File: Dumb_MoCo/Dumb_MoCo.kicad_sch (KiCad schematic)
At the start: 18 parts, among them U1 VNH7070AS

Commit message: Completed layout before review
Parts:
- removed C3: 220uF, symbol Device:C
- removed Conn3: Molex_SL_02, symbol MRDT_Connectors:Molex_SL_02
- removed Conn4: Molex_SL_03, symbol MRDT_Connectors:Molex_SL_03
- added C3: 270uF, Capacitor_THT:CP_Radial_D8.0mm_P3.50mm, symbol Device:C_Polarized
- added C4: 10nF, Capacitor_SMD:C_0603_1608Metric_Pad1.08x0.95mm_HandSolder, symbol Device:C
- added Conn3: Molex_SL_05, MRDT_Connectors:MOLEX_SL_05_Horizontal, symbol MRDT_Connectors:Molex_SL_05
- C1, C2: footprint (none) -> Capacitor_SMD:C_0603_1608Metric_Pad1.08x0.95mm_HandSolder
- Conn1, Conn2: footprint (none) -> MRDT_Connectors:Square_Anderson_2_H_Side_By_Side
- U1: footprint (none) -> Package_SO:SOIC-16_3.9x9.9mm_P1.27mm
- V1, V2, V3, V4: footprint (none) -> MRDT_Drill_Holes:4_40_Hole
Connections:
- net +12V: now also C3.1
- net CS: now also C4.2, Conn3.2
- net GND: now also C3.2, C4.1
- net IN_A: now also Conn3.3
- net IN_B: now also Conn3.4
- net M-: now also Conn1.1 (GND), U1.10 (OUT_B), U1.7 (OUT_B)
- net PWM: now also Conn3.5
- net SEL: now also Conn3.1
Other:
- moved on the sheet: Conn1A, Conn1B, R1, R2, R3, R4, R5, R6, V4

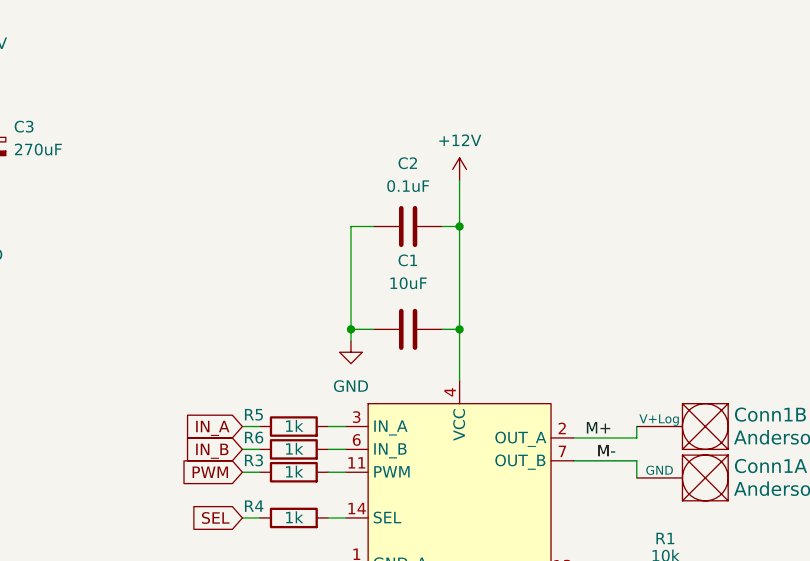
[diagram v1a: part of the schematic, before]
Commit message: Removed C1
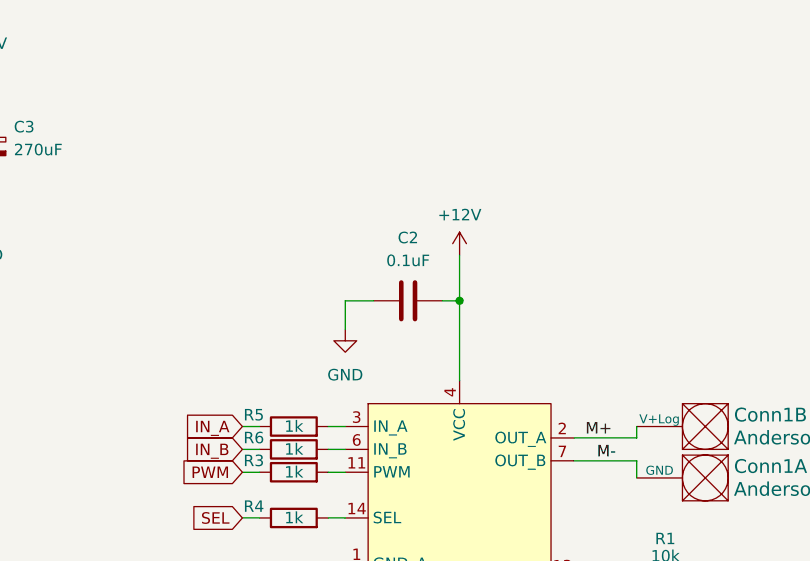
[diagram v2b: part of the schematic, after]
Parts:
- removed C1: 10uF, Capacitor_SMD:C_0603_1608Metric_Pad1.08x0.95mm_HandSolder, symbol Device:C
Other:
- moved on the sheet: C2
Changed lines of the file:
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@@
 	)
 	(junction
-		(at 92.71 46.355)
+		(at 92.71 54.61)
 		(diameter 0)
 		(color 0 0 0 0)
@@
 	)
 	(junction
-		(at 92.71 57.785)
-		(diameter 0)
-		(color 0 0 0 0)
-	)
-	(junction
-		(at 80.645 57.785)
-		(diameter 0)
-		(color 0 0 0 0)
-	)
-	(junction
 		(at 108.585 85.09)
 		(diameter 0)
@@
 	(wire
 		(pts
-			(xy 80.645 46.355) (xy 80.645 57.785)
-		)
-		(stroke
-			(width 0)
-			(type default)
-		)
-	)
-	(wire
-		(pts
 			(xy 78.105 71.12) (xy 80.01 71.12)
 		)
@@
 	(wire
 		(pts
-			(xy 92.71 57.785) (xy 92.71 63.5)
-		)
-		(stroke
-			(width 0)
-			(type default)
-		)
-	)
-	(wire
-		(pts
-			(xy 80.645 57.785) (xy 83.185 57.785)
-		)
-		(stroke
-			(width 0)
-			(type default)
-		)
-	)
-	(wire
-		(pts
 			(xy 74.93 83.82) (xy 74.93 86.36)
 		)
@@
 	(wire
 		(pts
-			(xy 80.645 57.785) (xy 80.645 59.055)
-		)
-		(stroke
-			(width 0)
-			(type default)
-		)
-	)
-	(wire
-		(pts
-			(xy 90.805 57.785) (xy 92.71 57.785)
-		)
-		(stroke
-			(width 0)
-			(type default)
-		)
-	)
-	(wire
-		(pts
-			(xy 92.71 41.275) (xy 92.71 46.355)
+			(xy 80.01 54.61) (xy 80.01 57.785)
+		)
+		(stroke
+			(width 0)
+			(type default)
+		)
+	)
+	(wire
+		(pts
+			(xy 92.71 49.53) (xy 92.71 54.61)
 		)
 		(stroke
@@
 	(wire
 		(pts
-			(xy 90.805 46.355) (xy 92.71 46.355)
+			(xy 90.805 54.61) (xy 92.71 54.61)
 		)
 		(stroke
@@
 	(wire
 		(pts
+			(xy 92.71 54.61) (xy 92.71 63.5)
+		)
+		(stroke
+			(width 0)
+			(type default)
+		)
+	)
+	(wire
+		(pts
 			(xy 105.41 85.09) (xy 108.585 85.09)
 		)
@@
 	(wire
 		(pts
-			(xy 83.185 46.355) (xy 80.645 46.355)
+			(xy 83.185 54.61) (xy 80.01 54.61)
 		)
 		(stroke
@@
 		(pts
 			(xy 78.105 68.58) (xy 80.01 68.58)
-		)
-		(stroke
-			(width 0)
-			(type default)
-		)
-	)
-	(wire
-		(pts
-			(xy 92.71 46.355) (xy 92.71 57.785)
 		)
 		(stroke
@@
 	(symbol
 		(lib_id "Device:C")
-		(at 86.995 57.785 90)
+		(at 86.995 54.61 90)
 		(unit 1)
 		(exclude_from_sim no)
@@
 		(dnp no)
 		(fields_autoplaced yes)
-		(property "Reference" "C1"
+		(property "Reference" "C2"
+			(at 86.995 47.625 90)
+			(effects
+				(font
+					(size 1.27 1.27)
+				)
+			)
+		)
+		(property "Value" "0.1uF"
 			(at 86.995 50.165 90)
 			(effects
@@
 			)
 		)
-		(property "Value" "10uF"
-			(at 86.995 52.705 90)
-			(effects
-				(font
-					(size 1.27 1.27)
-				)
-			)
-		)
 		(property "Footprint" "Capacitor_SMD:C_0603_1608Metric_Pad1.08x0.95mm_HandSolder"
-			(at 90.805 56.8198 0)
+			(at 90.805 53.6448 0)
 			(effects
 				(font
@@
 		)
 		(property "Datasheet" "~"
-			(at 86.995 57.785 0)
+			(at 86.995 54.61 0)
 			(effects
 				(font
@@
 		)
 		(property "Description" ""
-			(at 86.995 57.785 0)
-			(effects
-				(font
-					(size 1.27 1.27)
-				)
-				(hide yes)
-			)
-		)
-		(pin "1"
-		)
-		(pin "2"
-		)
-		(instances
-			(project "Dumb_MoCo"
-				(path "/e8f67502-d0e6-4aae-8b76-a782f13abdd3"
-					(reference "C1")
-					(unit 1)
-				)
-			)
-		)
-	)
-	(symbol
-		(lib_id "Device:C")
-		(at 86.995 46.355 90)
-		(unit 1)
-		(exclude_from_sim no)
-		(in_bom yes)
-		(on_board yes)
-		(dnp no)
-		(fields_autoplaced yes)
-		(property "Reference" "C2"
-			(at 86.995 39.37 90)
-			(effects
-				(font
-					(size 1.27 1.27)
-				)
-			)
-		)
-		(property "Value" "0.1uF"
-			(at 86.995 41.91 90)
-			(effects
-				(font
-					(size 1.27 1.27)
-				)
-			)
-		)
-		(property "Footprint" "Capacitor_SMD:C_0603_1608Metric_Pad1.08x0.95mm_HandSolder"
-			(at 90.805 45.3898 0)
-			(effects
-				(font
-					(size 1.27 1.27)
-				)
-				(hide yes)
-			)
-		)
-		(property "Datasheet" "~"
-			(at 86.995 46.355 0)
-			(effects
-				(font
-					(size 1.27 1.27)
-				)
-				(hide yes)
-			)
-		)
-		(property "Description" ""
-			(at 86.995 46.355 0)
+			(at 86.995 54.61 0)
 			(effects
 				(font
@@
 	(symbol
 		(lib_id "power:+12V")
-		(at 92.71 41.275 0)
+		(at 92.71 49.53 0)
 		(unit 1)
 		(exclude_from_sim no)
@@
 		(fields_autoplaced yes)
 		(property "Reference" "#PWR02"
+			(at 92.71 53.34 0)
+			(effects
+				(font
+					(size 1.27 1.27)
+				)
+				(hide yes)
+			)
+		)
+		(property "Value" "+12V"
 			(at 92.71 45.085 0)
 			(effects
@@
 					(size 1.27 1.27)
 				)
-				(hide yes)
-			)
-		)
-		(property "Value" "+12V"
-			(at 92.71 36.83 0)
-			(effects
-				(font
-					(size 1.27 1.27)
-				)
 			)
 		)
 		(property "Footprint" ""
-			(at 92.71 41.275 0)
+			(at 92.71 49.53 0)
 			(effects
 				(font
@@
 		)
 		(property "Datasheet" ""
-			(at 92.71 41.275 0)
+			(at 92.71 49.53 0)
 			(effects
 				(font
@@
 		)
 		(property "Description" ""
-			(at 92.71 41.275 0)
+			(at 92.71 49.53 0)
 			(effects
 				(font
@@
 	(symbol
 		(lib_id "power:GND")
-		(at 80.645 59.055 0)
+		(at 80.01 57.785 0)
 		(unit 1)
 		(exclude_from_sim no)
@@
 		(dnp no)
 		(property "Reference" "#PWR01"
-			(at 80.645 65.405 0)
+			(at 80.01 64.135 0)
 			(effects
 				(font
@@
 		)
 		(property "Value" "GND"
-			(at 80.645 64.135 0)
+			(at 80.01 62.865 0)
 			(effects
 				(font
@@
 		)
 		(property "Footprint" ""
-			(at 80.645 59.055 0)
+			(at 80.01 57.785 0)
 			(effects
 				(font
@@
 		)
 		(property "Datasheet" ""
-			(at 80.645 59.055 0)
+			(at 80.01 57.785 0)
 			(effects
 				(font
@@
 		)
 		(property "Description" ""
-			(at 80.645 59.055 0)
-			(effects
-				(font
+			(at 80.01 57.785 0)
+			(effects
+				(font

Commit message: Added Chamber Ult Silkscreen
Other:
- moved on the sheet: C2, C4, Conn1A, Conn1B, Conn3, R1, R2, R3, R4, R5, R6, U1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

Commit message: Started on layout
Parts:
- removed V1, V2, V3, V4: Via, MRDT_Drill_Holes:4_40_Hole, symbol MRDT_Drill_Holes:Via

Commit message: Finished layout draft
made anderson and SL vertical
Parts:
- Conn2: footprint MRDT_Connectors:Square_Anderson_2_H_Side_By_Side -> MRDT_Connectors:Square_Anderson_2_V_Side_By_Side
- Conn3: footprint MRDT_Connectors:MOLEX_SL_05_Horizontal -> MRDT_Connectors:MOLEX_SL_05_Vertical
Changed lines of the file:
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@@
 			)
 		)
-		(property "Footprint" "MRDT_Connectors:Square_Anderson_2_H_Side_By_Side"
+		(property "Footprint" "MRDT_Connectors:Square_Anderson_2_V_Side_By_Side"
 			(at 23.495 59.69 0)
 			(effects
@@
 			)
 		)
-		(property "Footprint" "MRDT_Connectors:MOLEX_SL_05_Horizontal"
+		(property "Footprint" "MRDT_Connectors:MOLEX_SL_05_Vertical"
 			(at 38.1 68.58 0)
 			(effects
@@
 			)
 		)
-		(property "Footprint" "MRDT_Connectors:Square_Anderson_2_H_Side_By_Side"
+		(property "Footprint" "MRDT_Connectors:Square_Anderson_2_V_Side_By_Side"
 			(at 23.495 48.26 0)
 			(effects

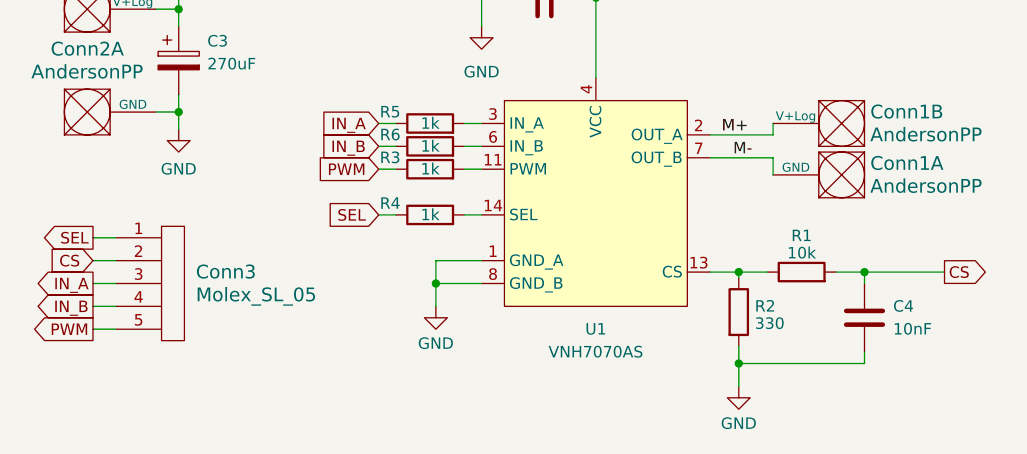
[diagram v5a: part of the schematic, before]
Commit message: Flipped VNH and reordered SL
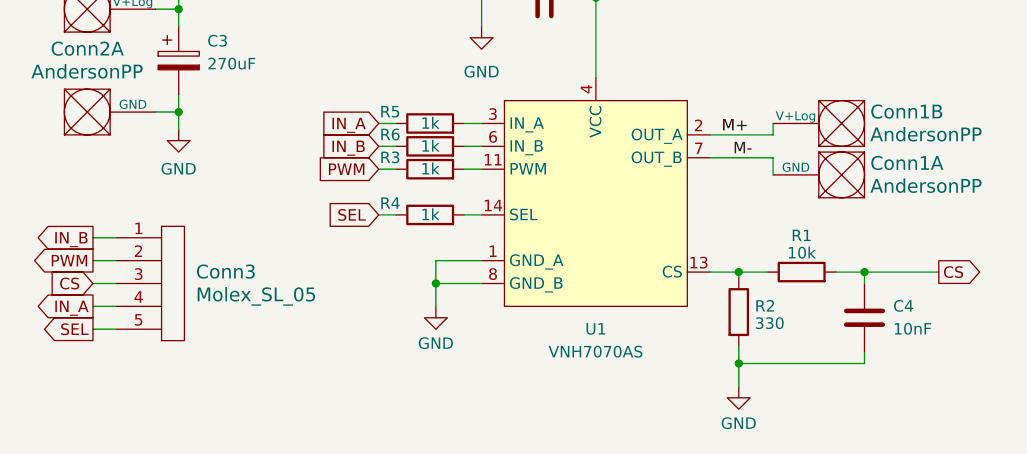
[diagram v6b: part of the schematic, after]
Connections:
- net CS: now also Conn3.3; no longer Conn3.2
- net IN_A: now also Conn3.4; no longer Conn3.3
- net IN_B: now also Conn3.1; no longer Conn3.4
- net PWM: now also Conn3.2; no longer Conn3.5
- net SEL: now also Conn3.5; no longer Conn3.1
